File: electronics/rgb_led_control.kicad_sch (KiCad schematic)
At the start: 7 parts, among them J1 rgb_led_conn, Q3 N-MOS, Q4 N-MOS, Q5 N-MOS

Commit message: from dell
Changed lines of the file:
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@@
 	(wire
 		(pts
-			(xy 71.12 100.33) (xy 77.47 100.33)
+			(xy 72.39 100.33) (xy 77.47 100.33)
 		)
 		(stroke
@@
 	(hierarchical_label "LED_B"
 		(shape input)
-		(at 71.12 100.33 180)
+		(at 72.39 100.33 180)
 		(fields_autoplaced yes)
 		(effects

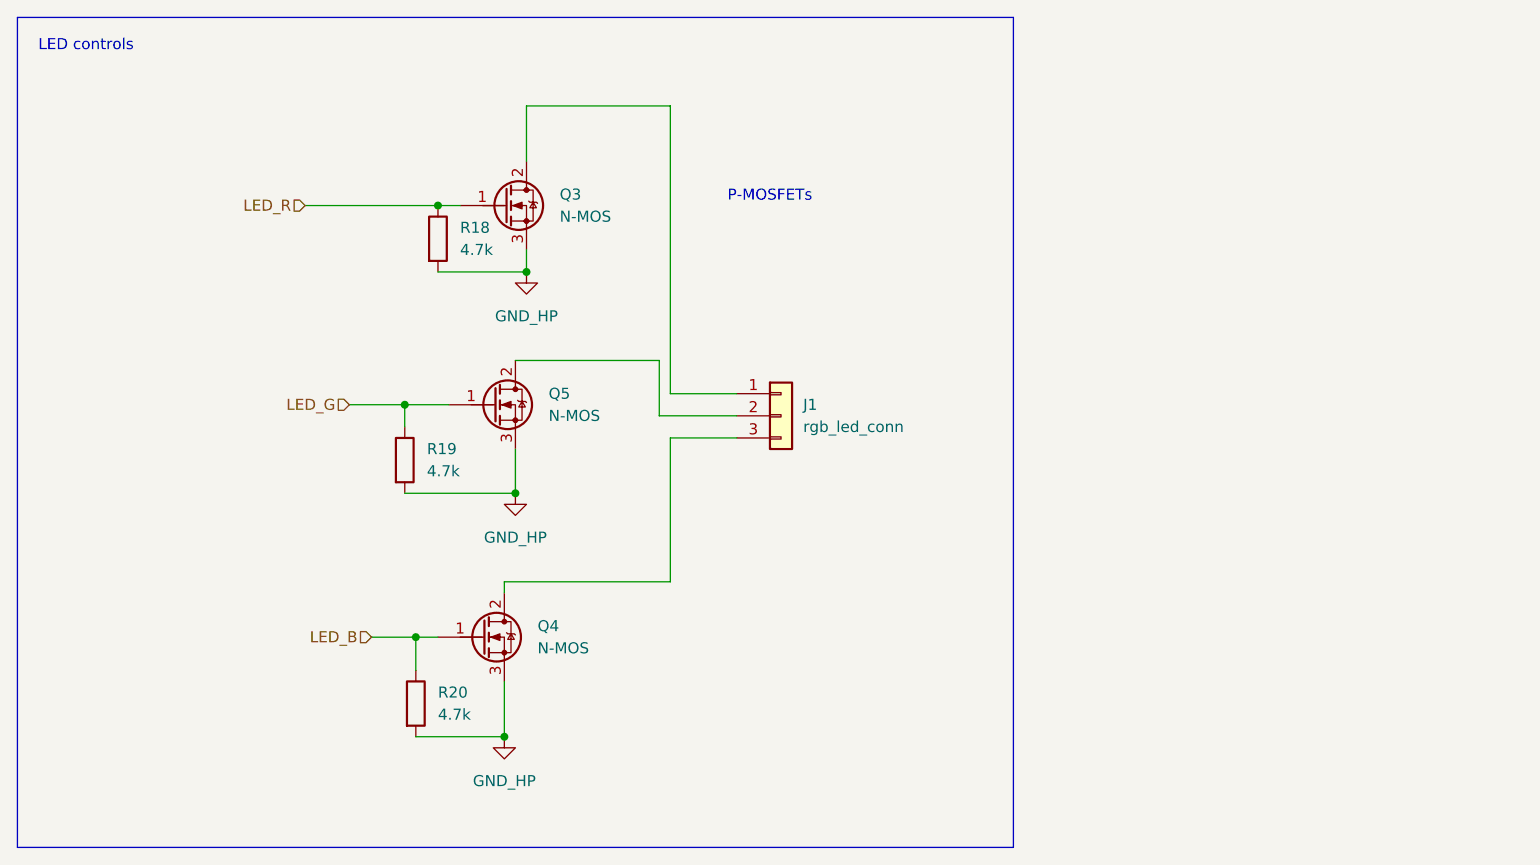
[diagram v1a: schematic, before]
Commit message: capacitors added. universal dc/dc converters
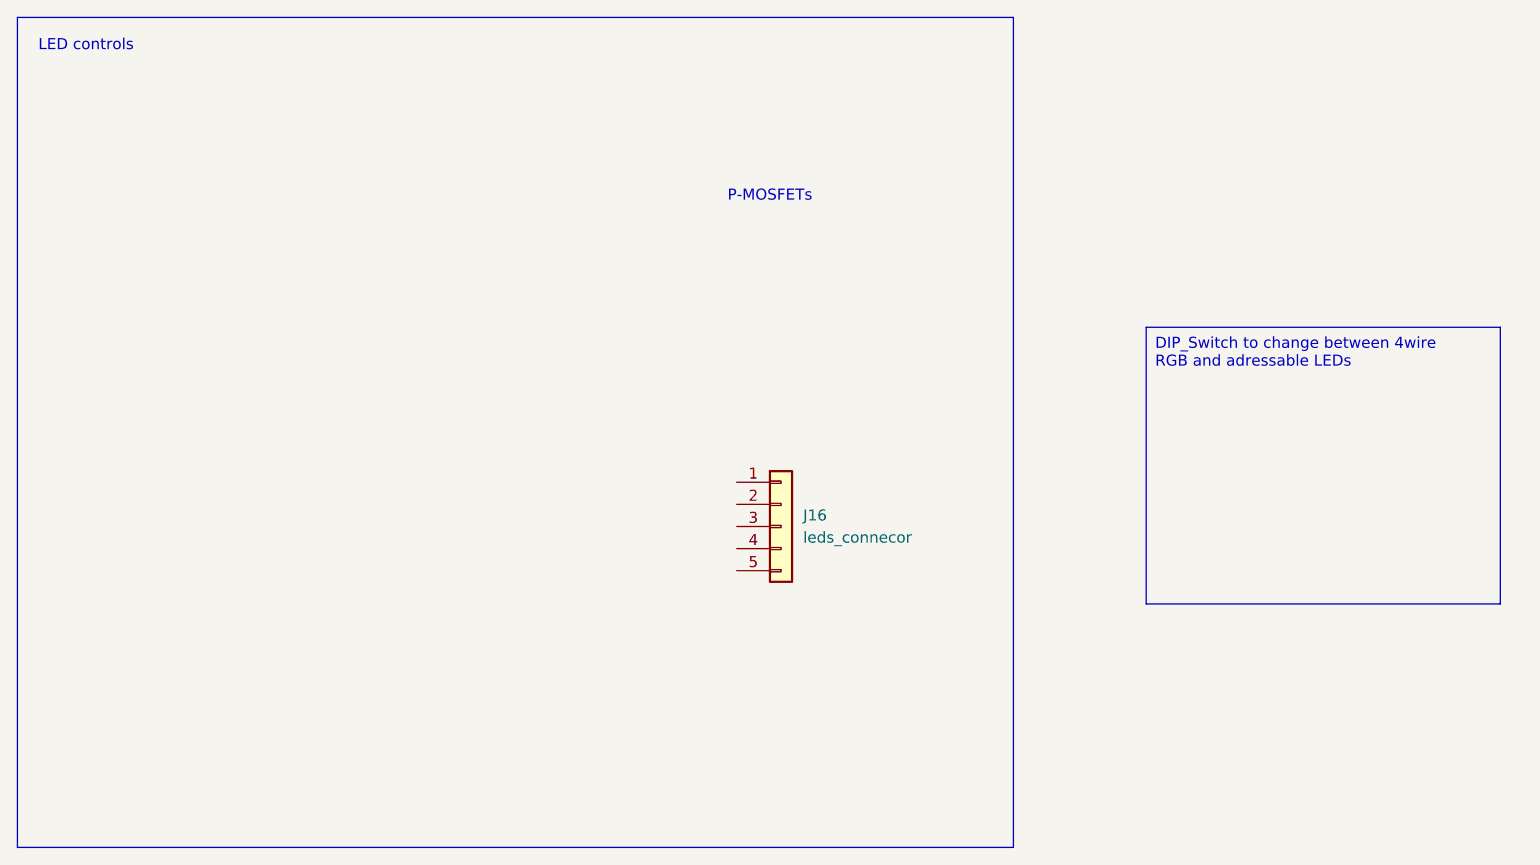
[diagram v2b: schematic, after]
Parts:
- removed J1: rgb_led_conn, TerminalBlock:TerminalBlock_Xinya_XY308-2.54-3P_1x03_P2.54mm_Horizontal, symbol Connector_Generic:Conn_01x03
- removed Q3, Q4, Q5: N-MOS, Package_TO_SOT_SMD:SOT-23, symbol Transistor_FET:BSP129
- removed R18, R19, R20: 4.7k, Resistor_SMD:R_0805_2012Metric_Pad1.20x1.40mm_HandSolder, symbol Device:R
- added J16: leds_connecor, TerminalBlock:TerminalBlock_Xinya_XY308-2.54-5P_1x05_P2.54mm_Horizontal, symbol Connector_Generic:Conn_01x05
